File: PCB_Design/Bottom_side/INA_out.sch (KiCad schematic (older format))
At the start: 4 parts

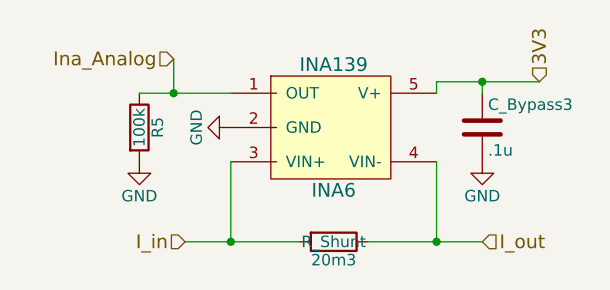
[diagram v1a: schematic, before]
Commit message: Updated PCB structure tree
Full_PCB now includes bottom and top layer hierarchical sheets
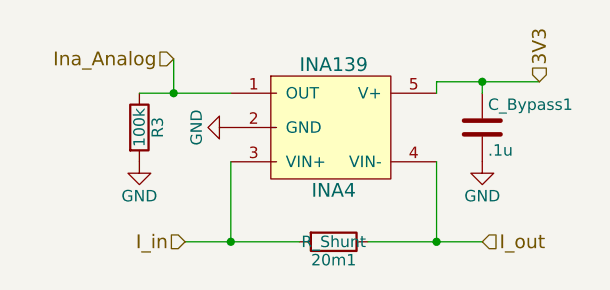
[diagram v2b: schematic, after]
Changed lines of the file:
@@
 LIBS:power
 LIBS:device
-LIBS:switches
-LIBS:relays
-LIBS:motors
 LIBS:transistors
 LIBS:conn
@@
 LIBS:contrib
 LIBS:valves
-LIBS:Bottom_side-cache
+LIBS:Full_PCB-cache
 EELAYER 25 0
 EELAYER END
 $Descr A4 11693 8268
 encoding utf-8
-Sheet 15 26
+Sheet 13 26
 Title "INA139 & Voltage Divider for Voltage Measurement"
 Date "2017-06-14"
@@
 AR Path="/5A57B48D/5A57F945/5A5826FA/5A684513" Ref="R3"  Part="1"
 AR Path="/5A57B48D/5A57F945/5A68448E/5A684513" Ref="R4"  Part="1"
-F 0 "R5" V 2580 1750 50  0000 C CNN
+F 0 "R3" V 2580 1750 50  0000 C CNN
 F 1 "100k" V 2500 1750 50  0000 C CNN
 F 2 "Resistors_SMD:R_0603" V 2430 1750 50  0001 C CNN
@@
 AR Path="/5A57B48D/5A57F945/5A5826FA/5A684514" Ref="20m1"  Part="1"
 AR Path="/5A57B48D/5A57F945/5A68448E/5A684514" Ref="20m2"  Part="1"
-F 0 "20m3" V 3430 2250 50  0000 C CNN
+F 0 "20m1" V 3430 2250 50  0000 C CNN
 F 1 "R_Shunt" V 3350 2250 50  0000 C CNN
 F 2 "Resistors_SMD:R_0805" V 3280 2250 50  0001 C CNN
@@
 AR Path="/5A57B48D/5A57F945/5A5826FA/5A684515" Ref="C_Bypass1"  Part="1"
 AR Path="/5A57B48D/5A57F945/5A68448E/5A684515" Ref="C_Bypass2"  Part="1"
-F 0 "C_Bypass3" H 4025 1850 50  0000 L CNN
+F 0 "C_Bypass1" H 4025 1850 50  0000 L CNN
 F 1 ".1u" H 4025 1650 50  0000 L CNN
 F 2 "Capacitors_SMD:C_0603" H 4038 1600 50  0001 C CNN
@@
 Connection ~ 4000 1550
 $Comp
-L GND #PWR056
+L GND #PWR050
 U 1 1 5A684516
 P 4000 1900
-AR Path="/5A57B48D/5A57F945/5A6847B9/5A684516" Ref="#PWR056"  Part="1"
-AR Path="/5A57B48D/5A57F945/5A5826FA/5A684516" Ref="#PWR050"  Part="1"
-AR Path="/5A57B48D/5A57F945/5A68448E/5A684516" Ref="#PWR053"  Part="1"
-F 0 "#PWR056" H 4000 1650 50  0001 C CNN
+AR Path="/5A57B48D/5A57F945/5A6847B9/5A684516" Ref="#PWR050"  Part="1"
+AR Path="/5A57B48D/5A57F945/5A5826FA/5A684516" Ref="#PWR044"  Part="1"
+AR Path="/5A57B48D/5A57F945/5A68448E/5A684516" Ref="#PWR047"  Part="1"
+F 0 "#PWR044" H 4000 1650 50  0001 C CNN
 F 1 "GND" H 4000 1750 50  0000 C CNN
 F 2 "" H 4000 1900 50  0001 C CNN
@@
 $EndComp
 $Comp
-L GND #PWR057
+L GND #PWR051
 U 1 1 5A684517
 P 2900 1750
-AR Path="/5A57B48D/5A57F945/5A6847B9/5A684517" Ref="#PWR057"  Part="1"
-AR Path="/5A57B48D/5A57F945/5A5826FA/5A684517" Ref="#PWR051"  Part="1"
-AR Path="/5A57B48D/5A57F945/5A68448E/5A684517" Ref="#PWR054"  Part="1"
-F 0 "#PWR057" H 2900 1500 50  0001 C CNN
+AR Path="/5A57B48D/5A57F945/5A6847B9/5A684517" Ref="#PWR051"  Part="1"
+AR Path="/5A57B48D/5A57F945/5A5826FA/5A684517" Ref="#PWR045"  Part="1"
+AR Path="/5A57B48D/5A57F945/5A68448E/5A684517" Ref="#PWR048"  Part="1"
+F 0 "#PWR045" H 2900 1500 50  0001 C CNN
 F 1 "GND" H 2900 1600 50  0000 C CNN
 F 2 "" H 2900 1750 50  0001 C CNN
@@
 AR Path="/5A57B48D/5A57F945/5A5826FA/5A684518" Ref="INA4"  Part="1"
 AR Path="/5A57B48D/5A57F945/5A68448E/5A684518" Ref="INA5"  Part="1"
-F 0 "INA6" H 3350 1475 60  0000 C CNN
+F 0 "INA4" H 3350 1475 60  0000 C CNN
 F 1 "INA139" H 3350 2025 60  0000 C CNN
 F 2 "TO_SOT_Packages_SMD:SOT-23-5" H 3225 1800 60  0001 C CNN
@@
 I_out
 $Comp
-L GND #PWR058
+L GND #PWR052
 U 1 1 5A684519
 P 2500 1900
-AR Path="/5A57B48D/5A57F945/5A6847B9/5A684519" Ref="#PWR058"  Part="1"
-AR Path="/5A57B48D/5A57F945/5A5826FA/5A684519" Ref="#PWR052"  Part="1"
-AR Path="/5A57B48D/5A57F945/5A68448E/5A684519" Ref="#PWR055"  Part="1"
-F 0 "#PWR058" H 2500 1650 50  0001 C CNN
+AR Path="/5A57B48D/5A57F945/5A6847B9/5A684519" Ref="#PWR052"  Part="1"
+AR Path="/5A57B48D/5A57F945/5A5826FA/5A684519" Ref="#PWR046"  Part="1"
+AR Path="/5A57B48D/5A57F945/5A68448E/5A684519" Ref="#PWR049"  Part="1"
+F 0 "#PWR046" H 2500 1650 50  0001 C CNN
 F 1 "GND" H 2500 1750 50  0000 C CNN
 F 2 "" H 2500 1900 50  0001 C CNN
